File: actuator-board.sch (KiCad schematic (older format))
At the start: 23 parts, among them U1 STM32F302K8U6, U2 MCP1703, U3 MAX3051, X1 16MHz 10ppm

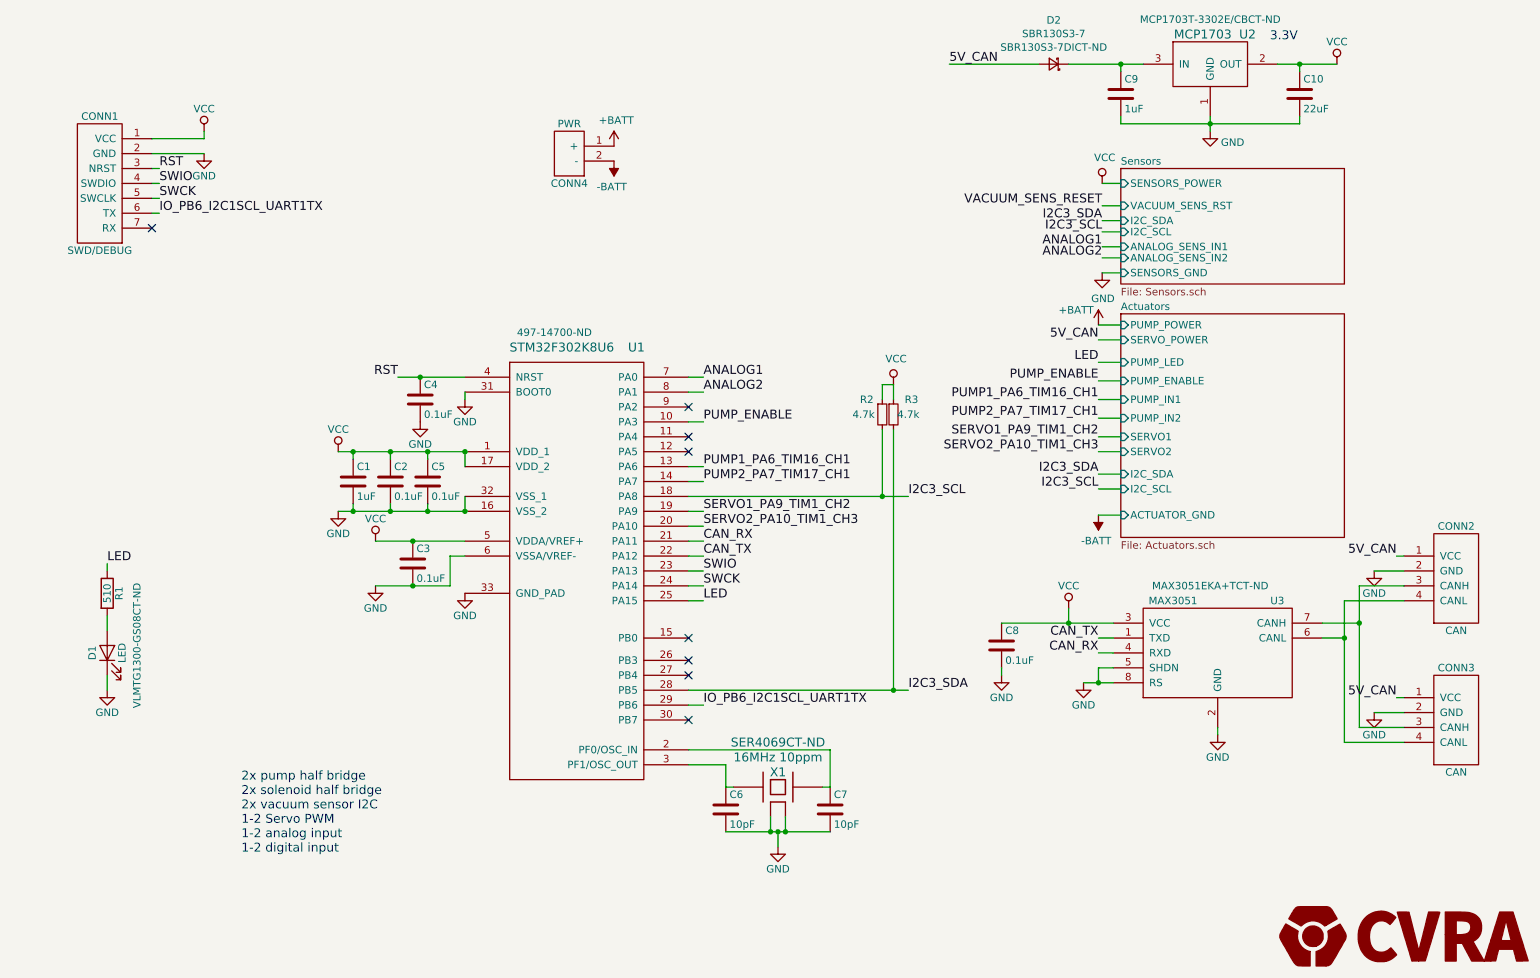
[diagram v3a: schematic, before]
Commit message: Correct schematics after review
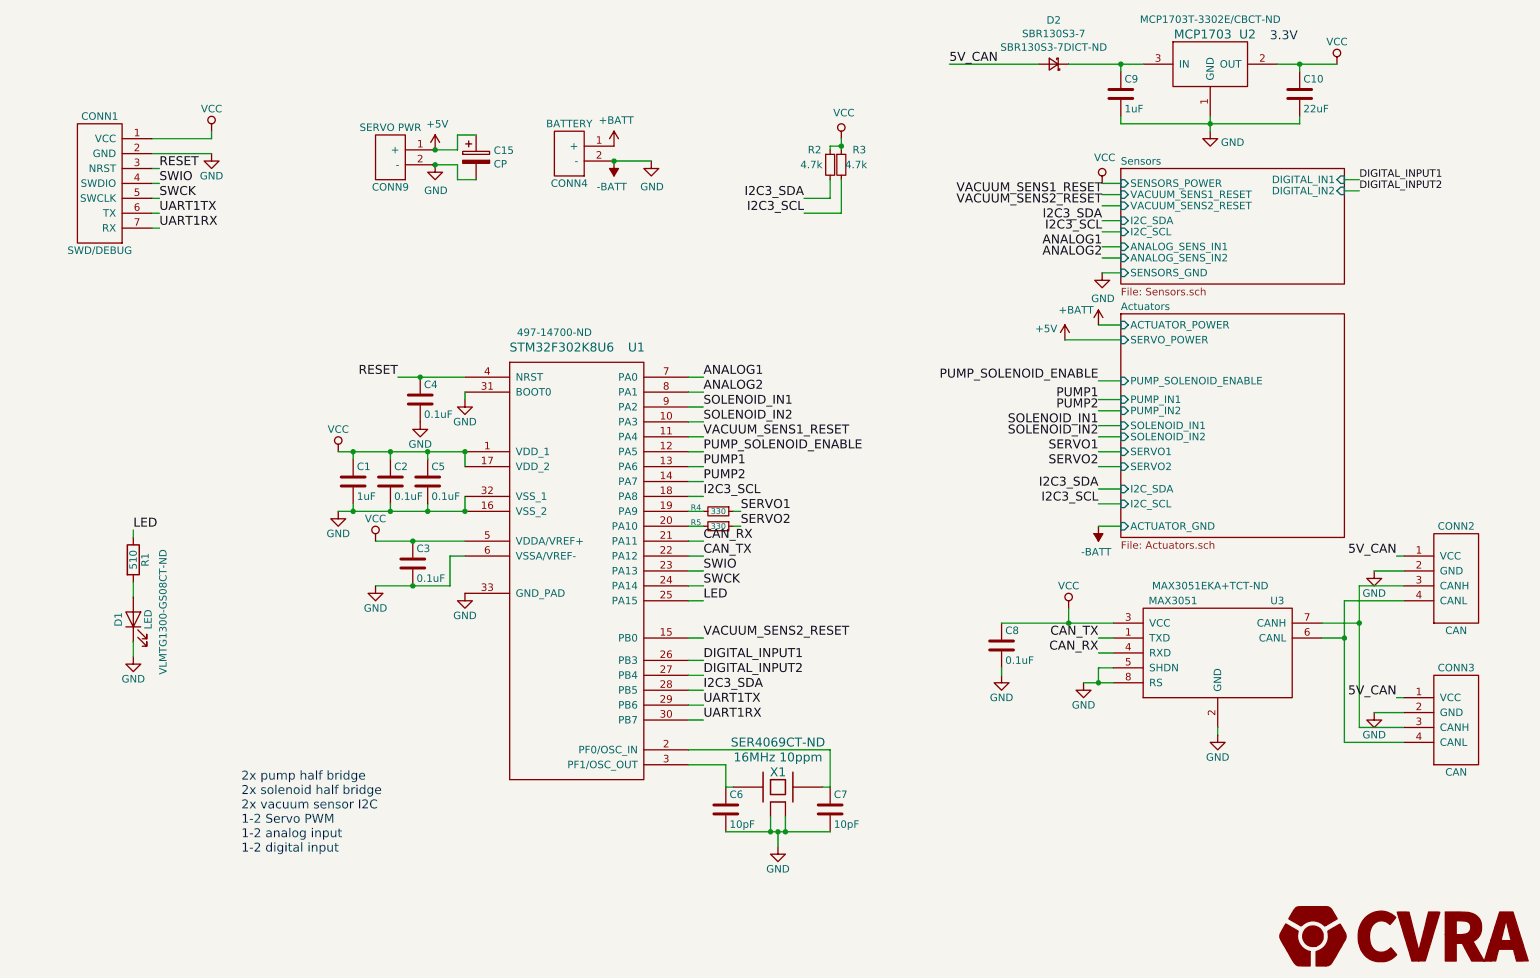
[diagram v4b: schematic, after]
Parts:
- added C15: CP, symbol Device:CP
- added CONN9: SERVO PWR, MODULE, symbol _connectors:PWR
- added R4, R5: 330, symbol Device:R_Small
- CONN4: value PWR -> BATTERY
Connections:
- net GND is gone; now on net -BATT: C1.2, C10.2, C2.2, C3.2, C4.2, C5.2, C6.2, C7.2, C8.2, C9.2, CONN1.2 (GND), CONN1.MECH (GND), CONN2.2 (GND), CONN2.MECH (GND), CONN3.2 (GND), CONN3.MECH (GND), CONN4.MECH (GND), D1.1 (K), U1.16 (VSS_2), U1.31 (BOOT0), U1.32 (VSS_1), U1.33 (GND_PAD), U1.6 (VSSA/VREF-), U2.1 (GND), U3.2 (GND), U3.5 (SHDN), U3.8 (RS), X1.2 (case), X1.4 (case)
- net -BATT: now also C15.2, CONN9.2 (-), CONN9.MECH (GND)
- net I2C3_SCL: now also R3.2; no longer R2.2
- net I2C3_SDA: now also R2.2; no longer R3.2
- net VACUUM_SENS1_RESET: now reaches U1.11 (PA4)
- net PUMP_SOLENOID_ENABLE: now reaches U1.12 (PA5)
- net VACUUM_SENS2_RESET: now reaches U1.15 (PB0)
- net DIGITAL_INPUT1: now reaches U1.26 (PB3)
- net DIGITAL_INPUT2: now reaches U1.27 (PB4)
- net UART1RX: now reaches U1.30 (PB7)
- net UART1RX: now also CONN1.7 (RX)
- net SOLENOID_IN1: now reaches U1.9 (PA2)
- net IO_PB6_I2C1SCL_UART1TX renamed UART1TX
- net PUMP1_PA6_TIM16_CH1 renamed PUMP1
- net PUMP2_PA7_TIM17_CH1 renamed PUMP2
- net PUMP_ENABLE renamed SOLENOID_IN2
- net RST renamed RESET
- net SERVO1_PA9_TIM1_CH2: no longer names the net of U1.19 (PA9)
- net SERVO1_PA9_TIM1_CH2: now also R4.2
- net SERVO2_PA10_TIM1_CH3: no longer names the net of U1.20 (PA10)
- net SERVO2_PA10_TIM1_CH3: now also R5.2
- new net +5V: C15.1, CONN9.1 (+)
- new net SERVO1: R4.1
- new net SERVO2: R5.1
- no-connect marks 8 -> 0
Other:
- moved on the sheet: D1, R1

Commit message: Cleanup labels, motor placement, power labels
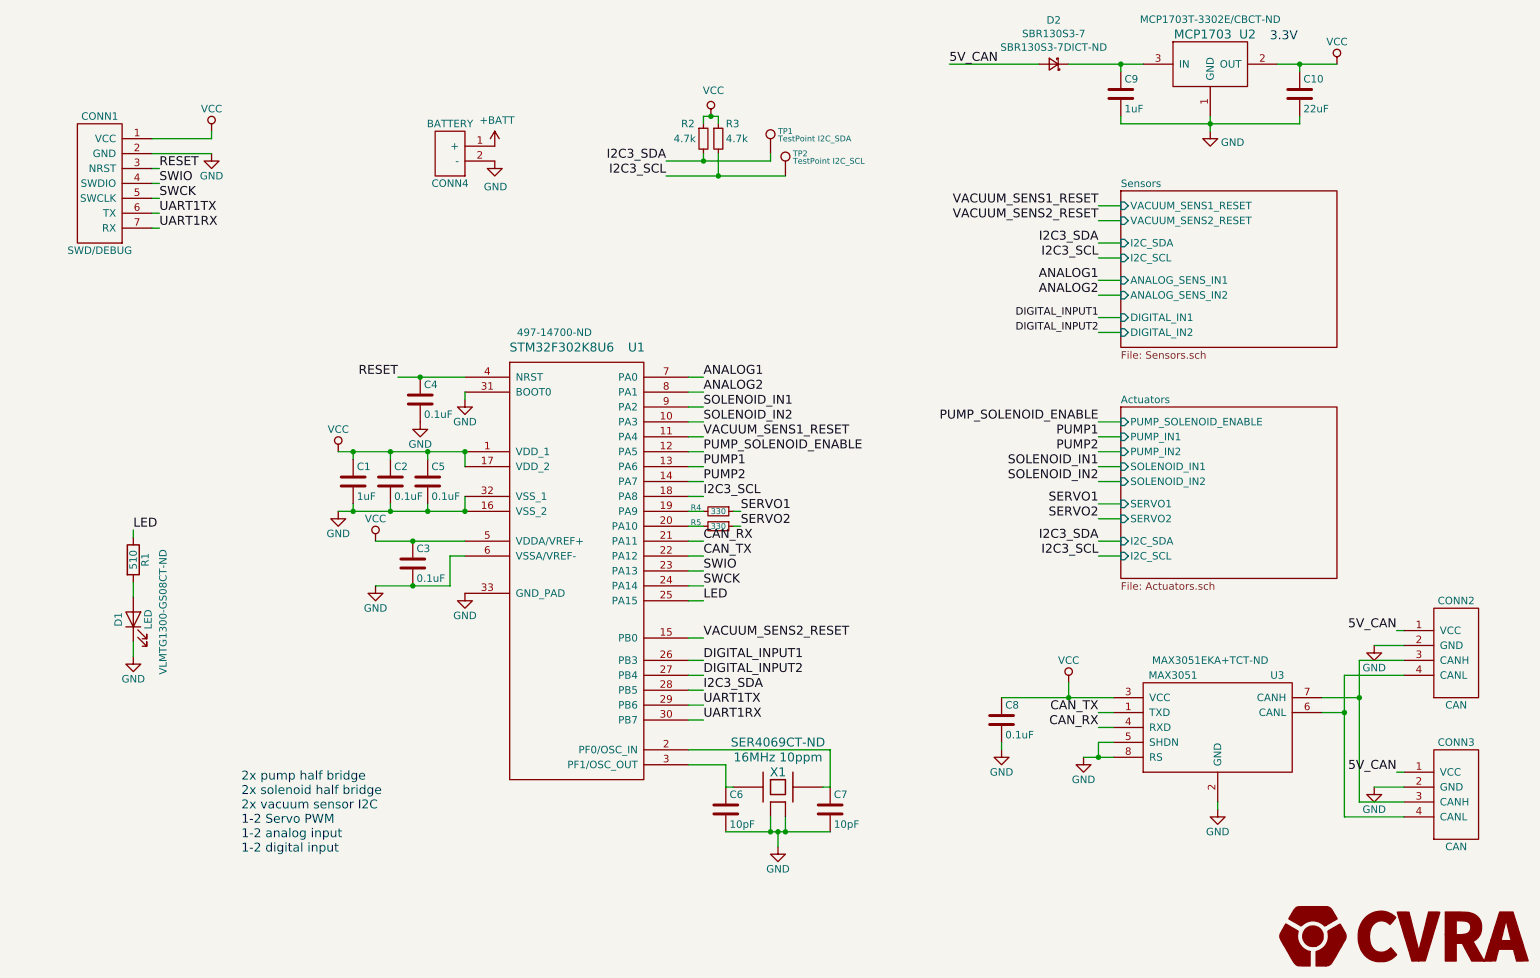
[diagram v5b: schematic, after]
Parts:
- removed C15: CP, symbol Device:CP
- removed CONN9: SERVO PWR, MODULE, symbol _connectors:PWR
- added TP1: TestPoint I2C_SDA, symbol Connector:TestPoint
- added TP2: TestPoint I2C_SCL, symbol Connector:TestPoint
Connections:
- net I2C3_SCL: now also TP2.1
- net I2C3_SDA: now also TP1.1
- net -BATT renamed GND
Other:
- moved on the sheet: C8, CONN2, CONN3, CONN4, R2, R3, U3
